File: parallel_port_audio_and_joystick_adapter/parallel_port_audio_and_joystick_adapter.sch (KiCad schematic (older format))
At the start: 6 parts, among them J1 DB25_Male, J2 DB9_Male, J3 AudioJack2

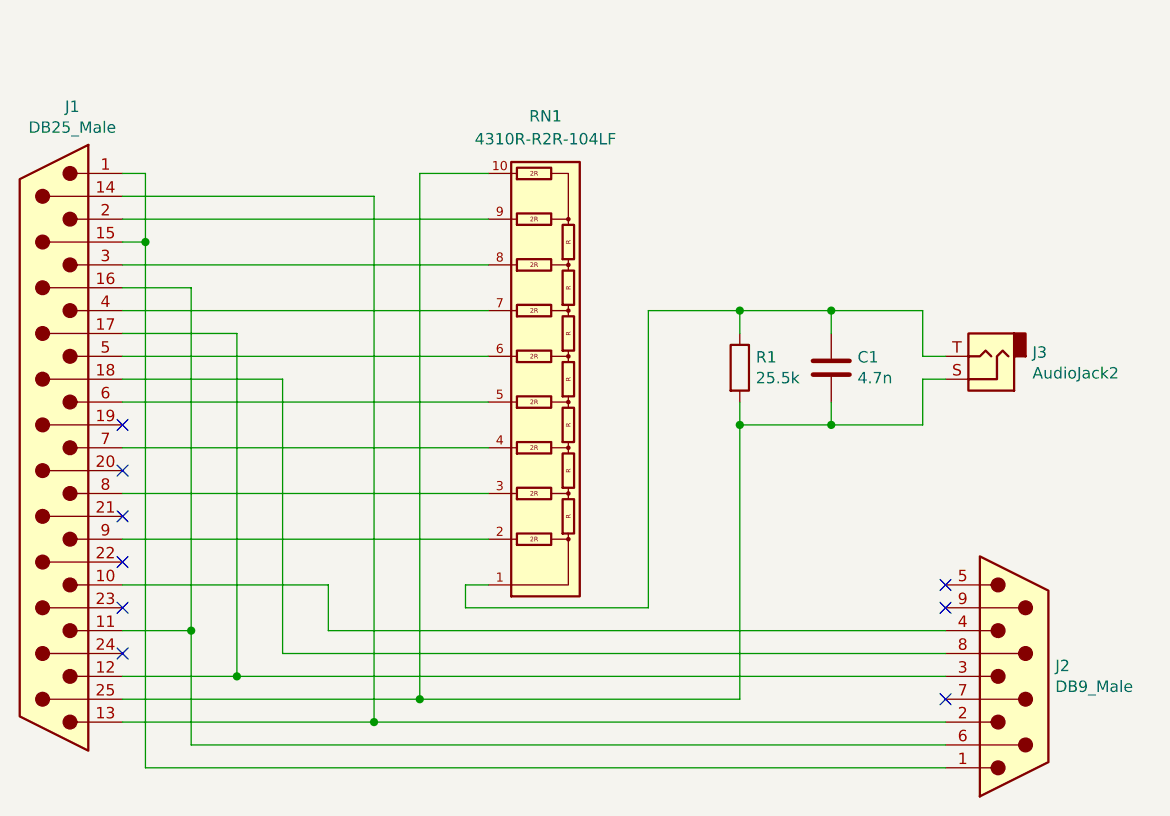
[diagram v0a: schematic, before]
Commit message: add resistors in series to prevent short circuit
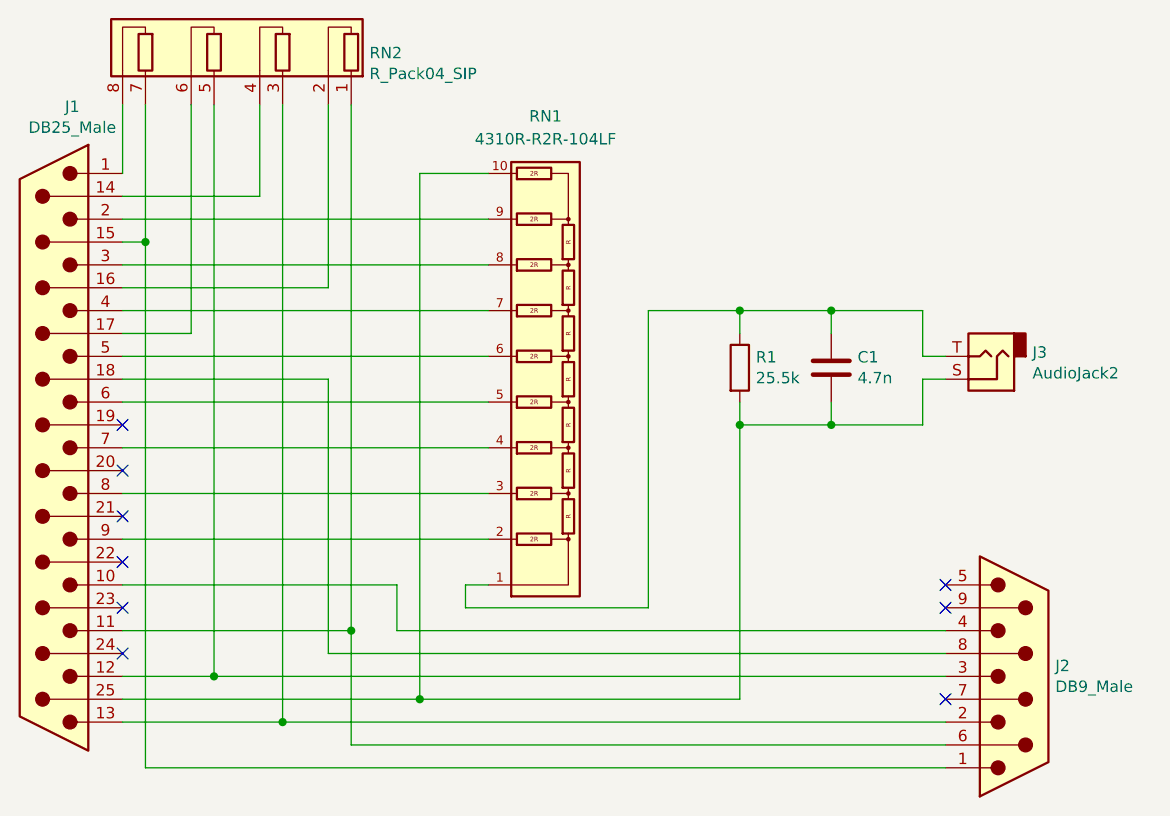
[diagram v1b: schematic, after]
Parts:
- added RN2: R_Pack04_SIP, Resistor_THT:R_Array_SIP8, symbol Device:R_Pack04_SIP
- J3: footprint Connector_Audio:Jack_3.5mm_CUI_SJ1-3533NG_Horizontal -> parallel_port_audio_and_joystick_adapter:Jack_3.5mm_CUI_SJ1-3525N_Horizontal
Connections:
- net at J1.15 (P15), J2.1: now also RN2.7 (R4.1); no longer J1.1
- net at J1.11, J2.6: now also RN2.1 (R1.1); no longer J1.16 (P16)
- net at J1.12, J2.3: now also RN2.5 (R3.1); no longer J1.17 (P17)
- net at J1.13, J2.2: now also RN2.3 (R2.1); no longer J1.14 (P14)
- new net: J1.1, RN2.8 (R4.2)
- new net: J1.14 (P14), RN2.4 (R2.2)
- new net: J1.16 (P16), RN2.2 (R1.2)
- new net: J1.17 (P17), RN2.6 (R3.2)
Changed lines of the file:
@@
 EESchema Schematic File Version 4
 LIBS:parallel_port_audio_and_joystick_adapter-cache
-EELAYER 26 0
+EELAYER 29 0
 EELAYER END
 $Descr A4 11693 8268
@@
 F 0 "J3" H 5820 3583 50  0000 R CNN
 F 1 "AudioJack2" H 5820 3674 50  0000 R CNN
-F 2 "Connector_Audio:Jack_3.5mm_CUI_SJ1-3533NG_Horizontal" H 6000 3600 50  0001 C CNN
+F 2 "parallel_port_audio_and_joystick_adapter:Jack_3.5mm_CUI_SJ1-3525N_Horizontal" H 6000 3600 50  0001 C CNN
 F 3 "~" H 6000 3600 50  0001 C CNN
 	1    6000 3600
@@
 NoConn ~ 5800 5100
 Wire Wire Line
-	2200 2800 2300 2800
-Wire Wire Line
 	2200 3100 2300 3100
 Wire Wire Line
-	2300 3100 2300 2800
-Wire Wire Line
-	2700 3500 2700 5000
-Wire Wire Line
 	5300 3400 5300 3500
 Wire Wire Line
@@
 	5700 3900 5700 3700
 Wire Wire Line
-	5800 5200 3300 5200
-Wire Wire Line
-	2900 3700 2900 4900
-Wire Wire Line
-	2700 5000 5800 5000
-Wire Wire Line
-	2500 5300 5800 5300
-Wire Wire Line
-	2200 3300 2500 3300
-Wire Wire Line
-	2200 3500 2700 3500
-Wire Wire Line
-	2200 3700 2900 3700
-Wire Wire Line
 	3500 2800 3500 5100
 Wire Wire Line
@@
 Wire Wire Line
 	2200 4400 3800 4400
-Wire Wire Line
-	3300 2900 3300 5200
-Wire Wire Line
-	2500 3300 2500 4800
-Wire Wire Line
-	2200 5000 2700 5000
-Connection ~ 2700 5000
-Wire Wire Line
-	2200 4800 2500 4800
-Connection ~ 2500 4800
-Wire Wire Line
-	2500 4800 2500 5300
 Wire Wire Line
 	2300 3100 2300 5400
@@
 Connection ~ 2300 3100
 Wire Wire Line
-	3100 4800 3100 4600
+	3400 4800 3400 4600
 Connection ~ 4900 3400
 Wire Wire Line
@@
 Connection ~ 4900 3900
 Wire Wire Line
-	2900 4900 5800 4900
-Wire Wire Line
-	3100 4600 2200 4600
-Wire Wire Line
-	3100 4800 5800 4800
-Wire Wire Line
 	3500 2800 3800 2800
 Connection ~ 3500 5100
@@
 Wire Wire Line
 	2200 5100 3500 5100
-Connection ~ 3300 5200
-Wire Wire Line
-	2200 5200 3300 5200
-Wire Wire Line
-	2200 2900 3300 2900
+$Comp
+L Device:R_Pack04_SIP RN2
+U 1 1 5CA9E6B0
+P 2700 2300
+F 0 "RN2" H 2120 2327 50  0000 R CNN
+F 1 "R_Pack04_SIP" H 2120 2236 50  0000 R CNN
+F 2 "Resistor_THT:R_Array_SIP8" V 3375 2300 50  0001 C CNN
+F 3 "http://www.vishay.com/docs/31509/csc.pdf" H 2700 2300 50  0001 C CNN
+	1    2700 2300
+	-1   0    0    -1
+$EndComp
+Wire Wire Line
+	2200 3500 2500 3500
+Wire Wire Line
+	2200 5000 2600 5000
+Wire Wire Line
+	3100 3700 3100 4900
+Wire Wire Line
+	3200 4800 3200 5300
+Connection ~ 2900 5200
+Wire Wire Line
+	2900 5200 5800 5200
+Wire Wire Line
+	2200 5200 2900 5200
+Wire Wire Line
+	2200 3300 3100 3300
+Connection ~ 2600 5000
+Wire Wire Line
+	2600 5000 5800 5000
+Wire Wire Line
+	2200 2900 2800 2900
+Wire Wire Line
+	3400 4800 5800 4800
+Wire Wire Line
+	2200 4600 3400 4600
+Connection ~ 3200 4800
+Wire Wire Line
+	3200 5300 5800 5300
+Wire Wire Line
+	2200 4800 3200 4800
+Wire Wire Line
+	3100 4900 5800 4900
+Wire Wire Line
+	2200 3700 3100 3700
+Wire Wire Line
+	3200 2500 3200 4800
+Wire Wire Line
+	3100 2500 3100 3300
+Wire Wire Line
+	2900 2500 2900 5200
+Wire Wire Line
+	2800 2500 2800 2900
+Wire Wire Line
+	2600 2500 2600 5000
+Wire Wire Line
+	2500 2500 2500 3500
+Wire Wire Line
+	2300 2500 2300 3100
+Wire Wire Line
+	2200 2500 2200 2800
 $EndSCHEMATC
